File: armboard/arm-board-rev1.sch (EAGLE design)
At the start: 37 parts, among them J2_12V ANDERSON_POWERPOLEPP45_PCB_HO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, J2_GND ANDERSON_POWERPOLEPP45_PCB_HO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, X1 53261-06

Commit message: finished routing, FINAL REV1 PENDING PEER REVIEW
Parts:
- removed H1: MOUNT-HOLE3.2, holes:MOUNT-HOLE3.2
- DECAP: value (none) -> 1uF
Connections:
- removed net N$5: MAX232_1.VCC, MAX232_DECAP_1.2
- net +3V3: now also MAX232_1.VCC, MAX232_DECAP_1.2
- net ENC_EI: now also U$1.PD1
- net ENC_EO: now also U$1.PD0
- net ENC_J1: now also U$1.PM2
- net ENC_J2: now also U$1.PM1
- net ENC_WI: now also U$1.PM3
- net ENC_WO: now also U$1.PL4
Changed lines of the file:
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@@
 <part name="ENC_J2" library="con-molex" deviceset="53?-03" device="261" value="53261-03"/>
 <part name="ENC_EI" library="con-molex" deviceset="53?-03" device="261" value="53261-03"/>
-<part name="DECAP" library="SparkFun-Capacitors" deviceset="100UF-25V-20%(PTH)" device=""/>
-<part name="H1" library="holes" deviceset="MOUNT-HOLE" device="3.2"/>
+<part name="DECAP" library="SparkFun-Capacitors" deviceset="100UF-25V-20%(PTH)" device="" value="1uF"/>
 <part name="H2" library="holes" deviceset="MOUNT-HOLE" device="3.2"/>
 <part name="GND7" library="SparkFun-Aesthetics" deviceset="GND" device=""/>
@@
 </segment>
 </net>
+<net name="ENC_J2" class="0">
+<segment>
+<pinref part="U$1" gate="G$1" pin="PM1"/>
+<wire x1="12.7" y1="38.1" x2="7.62" y2="38.1" width="0.1524" layer="91"/>
+<label x="7.62" y="38.1" size="1.016" layer="95" rot="R180" xref="yes"/>
+</segment>
+</net>
+<net name="ENC_J1" class="0">
+<segment>
+<pinref part="U$1" gate="G$1" pin="PM2"/>
+<wire x1="12.7" y1="35.56" x2="7.62" y2="35.56" width="0.1524" layer="91"/>
+<label x="7.62" y="35.56" size="1.016" layer="95" rot="R180" xref="yes"/>
+</segment>
+</net>
+<net name="ENC_EO" class="0">
+<segment>
+<pinref part="U$1" gate="G$1" pin="PD0"/>
+<wire x1="48.26" y1="88.9" x2="53.34" y2="88.9" width="0.1524" layer="91"/>
+<label x="53.34" y="88.9" size="1.016" layer="95" xref="yes"/>
+</segment>
+</net>
+<net name="ENC_EI" class="0">
+<segment>
+<pinref part="U$1" gate="G$1" pin="PD1"/>
+<wire x1="48.26" y1="86.36" x2="53.34" y2="86.36" width="0.1524" layer="91"/>
+<label x="53.34" y="86.36" size="1.016" layer="95" xref="yes"/>
+</segment>
+</net>
+<net name="ENC_WO" class="0">
+<segment>
+<pinref part="U$1" gate="G$1" pin="PL4"/>
+<wire x1="48.26" y1="33.02" x2="53.34" y2="33.02" width="0.1524" layer="91"/>
+<label x="53.34" y="33.02" size="1.016" layer="95" xref="yes"/>
+</segment>
+</net>
+<net name="ENC_WI" class="0">
+<segment>
+<pinref part="U$1" gate="G$1" pin="PM3"/>
+<wire x1="12.7" y1="33.02" x2="7.62" y2="33.02" width="0.1524" layer="91"/>
+<label x="7.62" y="33.02" size="1.016" layer="95" rot="R180" xref="yes"/>
+</segment>
+</net>
 </nets>
 </sheet>
@@
 <instance part="P+4" gate="1" x="22.86" y="48.26"/>
 <instance part="DECAP" gate="G$1" x="22.86" y="38.1"/>
-<instance part="H1" gate="G$1" x="-25.4" y="38.1"/>
 <instance part="H2" gate="G$1" x="-25.4" y="30.48"/>
 <instance part="GND7" gate="1" x="58.42" y="-7.62"/>
@@
 <pinref part="ENC_EI" gate="-2" pin="S"/>
 <label x="33.02" y="76.2" size="1.016" layer="95" rot="R180" xref="yes"/>
-<wire x1="35.56" y1="76.2" x2="33.02" y2="76.2" width="0.1524" layer="91"/>
-<wire x1="35.56" y1="76.2" x2="38.1" y2="76.2" width="0.1524" layer="91"/>
+<wire x1="33.02" y1="76.2" x2="38.1" y2="76.2" width="0.1524" layer="91"/>
 </segment>
 </net>
@@
 <pinref part="ENC_EI" gate="-3" pin="S"/>
 <pinref part="ENC_EO" gate="-3" pin="S"/>
-<wire x1="35.56" y1="73.66" x2="22.86" y2="73.66" width="0.1524" layer="91"/>
+<wire x1="38.1" y1="73.66" x2="22.86" y2="73.66" width="0.1524" layer="91"/>
 <wire x1="38.1" y1="60.96" x2="22.86" y2="60.96" width="0.1524" layer="91"/>
 <wire x1="22.86" y1="60.96" x2="22.86" y2="48.26" width="0.1524" layer="91"/>
@@
 <wire x1="22.86" y1="99.06" x2="22.86" y2="86.36" width="0.1524" layer="91"/>
 <junction x="22.86" y="86.36"/>
-<wire x1="35.56" y1="73.66" x2="38.1" y2="73.66" width="0.1524" layer="91"/>
+<pinref part="GND12" gate="1" pin="GND"/>
 </segment>
 </net>
@@
 <net name="T1OUT" class="0">
 <segment>
-<wire x1="134.62" y1="25.4" x2="124.46" y2="25.4" width="0.1524" layer="91"/>
 <pinref part="X1" gate="-1" pin="S"/>
 <pinref part="MAX232_1" gate="G$1" pin="T1OUT"/>
-<wire x1="106.68" y1="25.4" x2="119.38" y2="25.4" width="0.1524" layer="91"/>
+<wire x1="106.68" y1="25.4" x2="134.62" y2="25.4" width="0.1524" layer="91"/>
 <label x="124.46" y="25.4" size="1.016" layer="95"/>
-<wire x1="121.92" y1="25.4" x2="124.46" y2="25.4" width="0.1524" layer="91"/>
-<wire x1="121.92" y1="25.4" x2="119.38" y2="25.4" width="0.1524" layer="91"/>
 </segment>
 </net>
@@
 <segment>
 <pinref part="MAX232_1" gate="G$1" pin="R1IN"/>
-<wire x1="106.68" y1="22.86" x2="109.22" y2="22.86" width="0.1524" layer="91"/>
 <pinref part="X1" gate="-2" pin="S"/>
 <label x="124.46" y="22.86" size="1.016" layer="95"/>
-<wire x1="109.22" y1="22.86" x2="121.92" y2="22.86" width="0.1524" layer="91"/>
-<wire x1="134.62" y1="22.86" x2="129.54" y2="22.86" width="0.1524" layer="91"/>
-<wire x1="121.92" y1="22.86" x2="111.76" y2="22.86" width="0.1524" layer="91"/>
-<wire x1="121.92" y1="22.86" x2="129.54" y2="22.86" width="0.1524" layer="91"/>
-</segment>
-</net>
-<net name="N$5" class="0">
+<wire x1="134.62" y1="22.86" x2="106.68" y2="22.86" width="0.1524" layer="91"/>
+</segment>
+</net>
+<net name="+3V3" class="0">
 <segment>
 <pinref part="MAX232_1" gate="G$1" pin="VCC"/>
@@
 <wire x1="73.66" y1="38.1" x2="76.2" y2="38.1" width="0.1524" layer="91"/>
 <junction x="76.2" y="38.1"/>
-</segment>
-</net>
+<pinref part="+3V6" gate="G$1" pin="+3V3"/>
+</segment>
+</net>

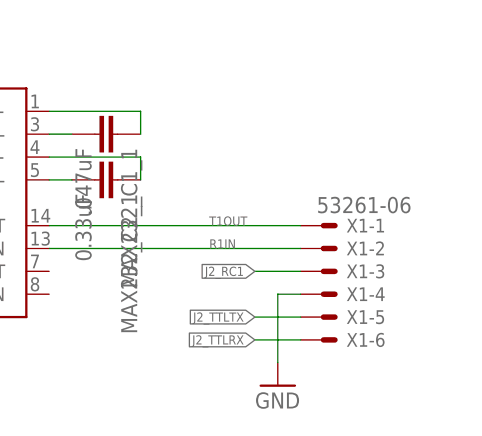
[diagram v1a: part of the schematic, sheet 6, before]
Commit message: added label/logo and 2 dio's to xbee
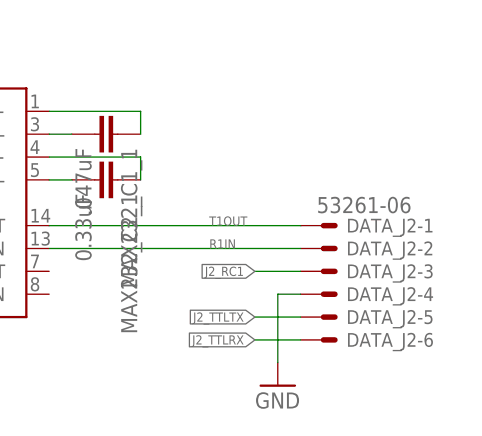
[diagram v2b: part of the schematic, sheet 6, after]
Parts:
- renumbered X1 to DATA_J2
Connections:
- net XB_DIO11: now also U$1.PM5
- net XB_DIO12: now also U$1.PM4
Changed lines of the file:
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@@
 <part name="GND9" library="SparkFun-Aesthetics" deviceset="GND" device=""/>
 <part name="GND11" library="SparkFun-Aesthetics" deviceset="GND" device=""/>
-<part name="X1" library="con-molex" deviceset="53?-06" device="261"/>
+<part name="DATA_J2" library="con-molex" deviceset="53?-06" device="261"/>
 <part name="MAX232_1" library="MRDT-Digital-ICs" deviceset="MAX3232" device="SO16"/>
 <part name="MAX232_C1_1" library="SparkFun-Capacitors" deviceset="CAP" device="1206" value=".047uF"/>
@@
 <wire x1="12.7" y1="33.02" x2="7.62" y2="33.02" width="0.1524" layer="91"/>
 <label x="7.62" y="33.02" size="1.016" layer="95" rot="R180" xref="yes"/>
+</segment>
+</net>
+<net name="XB_DIO12" class="0">
+<segment>
+<pinref part="U$1" gate="G$1" pin="PM4"/>
+<wire x1="12.7" y1="30.48" x2="7.62" y2="30.48" width="0.1524" layer="91"/>
+<label x="7.62" y="30.48" size="1.016" layer="95" rot="R180" xref="yes"/>
+</segment>
+</net>
+<net name="XB_DIO11" class="0">
+<segment>
+<pinref part="U$1" gate="G$1" pin="PM5"/>
+<wire x1="12.7" y1="27.94" x2="7.62" y2="27.94" width="0.1524" layer="91"/>
+<label x="7.62" y="27.94" size="1.016" layer="95" rot="R180" xref="yes"/>
 </segment>
 </net>
@@
 <instances>
 <instance part="GND15" gate="1" x="132.08" y="7.62"/>
-<instance part="X1" gate="-1" x="137.16" y="25.4"/>
-<instance part="X1" gate="-2" x="137.16" y="22.86"/>
-<instance part="X1" gate="-3" x="137.16" y="20.32"/>
-<instance part="X1" gate="-4" x="137.16" y="17.78"/>
-<instance part="X1" gate="-5" x="137.16" y="15.24"/>
-<instance part="X1" gate="-6" x="137.16" y="12.7"/>
+<instance part="DATA_J2" gate="-1" x="137.16" y="25.4"/>
+<instance part="DATA_J2" gate="-2" x="137.16" y="22.86"/>
+<instance part="DATA_J2" gate="-3" x="137.16" y="20.32"/>
+<instance part="DATA_J2" gate="-4" x="137.16" y="17.78"/>
+<instance part="DATA_J2" gate="-5" x="137.16" y="15.24"/>
+<instance part="DATA_J2" gate="-6" x="137.16" y="12.7"/>
 <instance part="MAX232_1" gate="G$1" x="78.74" y="15.24"/>
 <instance part="MAX232_C1_1" gate="G$1" x="111.76" y="35.56" rot="R270"/>
@@
 <wire x1="134.62" y1="17.78" x2="132.08" y2="17.78" width="0.1524" layer="91"/>
 <wire x1="132.08" y1="17.78" x2="132.08" y2="10.16" width="0.1524" layer="91"/>
-<pinref part="X1" gate="-4" pin="S"/>
+<pinref part="DATA_J2" gate="-4" pin="S"/>
 </segment>
 <segment>
@@
 <wire x1="134.62" y1="20.32" x2="129.54" y2="20.32" width="0.1524" layer="91"/>
 <label x="129.54" y="20.32" size="1.016" layer="95" rot="R180" xref="yes"/>
-<pinref part="X1" gate="-3" pin="S"/>
+<pinref part="DATA_J2" gate="-3" pin="S"/>
 </segment>
 </net>
@@
 <wire x1="134.62" y1="15.24" x2="129.54" y2="15.24" width="0.1524" layer="91"/>
 <label x="129.54" y="15.24" size="1.016" layer="95" rot="R180" xref="yes"/>
-<pinref part="X1" gate="-5" pin="S"/>
+<pinref part="DATA_J2" gate="-5" pin="S"/>
 </segment>
 </net>
@@
 <wire x1="134.62" y1="12.7" x2="129.54" y2="12.7" width="0.1524" layer="91"/>
 <label x="129.54" y="12.7" size="1.016" layer="95" rot="R180" xref="yes"/>
-<pinref part="X1" gate="-6" pin="S"/>
+<pinref part="DATA_J2" gate="-6" pin="S"/>
 </segment>
 </net>
 <net name="T1OUT" class="0">
 <segment>
-<pinref part="X1" gate="-1" pin="S"/>
+<pinref part="DATA_J2" gate="-1" pin="S"/>
 <pinref part="MAX232_1" gate="G$1" pin="T1OUT"/>
 <wire x1="106.68" y1="25.4" x2="134.62" y2="25.4" width="0.1524" layer="91"/>
@@
 <segment>
 <pinref part="MAX232_1" gate="G$1" pin="R1IN"/>
-<pinref part="X1" gate="-2" pin="S"/>
+<pinref part="DATA_J2" gate="-2" pin="S"/>
 <label x="124.46" y="22.86" size="1.016" layer="95"/>
 <wire x1="134.62" y1="22.86" x2="106.68" y2="22.86" width="0.1524" layer="91"/>

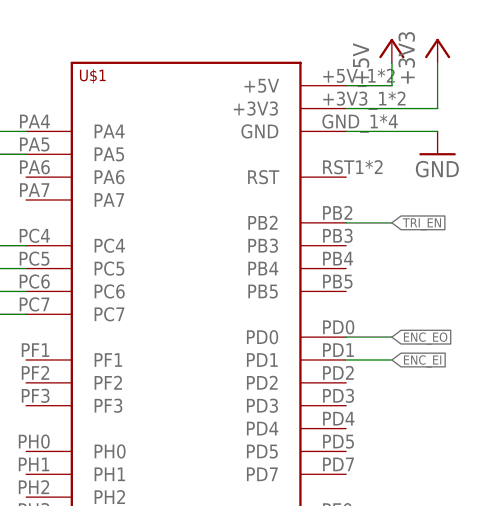
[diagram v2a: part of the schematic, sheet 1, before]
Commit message: moved xbee in a little, reviewed by Drue on arm ; REV 1 FINAL of Gripper Board
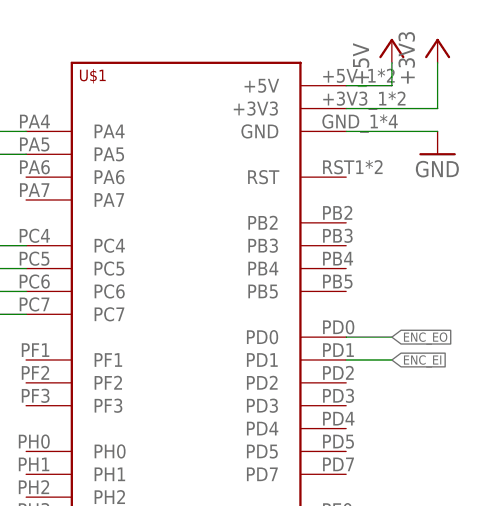
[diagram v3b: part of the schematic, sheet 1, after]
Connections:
- removed net TRI_EN: U$1.PB2
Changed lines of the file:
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@@
-</segment>
-</net>
-<net name="TRI_EN" class="0">
-<segment>
-<pinref part="U$1" gate="G$1" pin="PB2"/>
-<wire x1="48.26" y1="101.6" x2="53.34" y2="101.6" width="0.1524" layer="91"/>
-<label x="53.34" y="101.6" size="1.016" layer="95" xref="yes"/>
 </segment>
 </net>
